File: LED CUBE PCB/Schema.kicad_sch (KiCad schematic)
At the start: 1 part

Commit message: Push changes
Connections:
- net DIN8: now reaches TXB2.11 (B8)
- net DIN7: now reaches TXB2.12 (B7)
- net DIN6: now reaches TXB2.13 (B6)
- net DIN5: now reaches TXB2.14 (B5)
- net GND: now reaches TXB2.15 (GND)
- net DIN4: now reaches TXB2.17 (B4)
- net DIN3: now reaches TXB2.18 (B3)
- net DIN2: now reaches TXB2.19 (B2)
- net DIN1: now reaches TXB2.20 (B1)
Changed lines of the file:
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@@
 (kicad_sch (version 20230121) (generator eeschema)
   (paper "A4")
+  (wire (pts (xy 153.67 63.5) (xy 156.21 63.5))
+    (stroke (width 0) (type default))
+  )
+  (wire (pts (xy 153.67 52.07) (xy 153.67 53.34))
+    (stroke (width 0) (type default))
+  )
   (wire (pts (xy 120.65 57.15) (xy 109.22 57.15))
     (stroke (width 0) (type default))
   )
+  (wire (pts (xy 154.94 41.91) (xy 154.94 40.64))
+    (stroke (width 0) (type default))
+  )
+  (wire (pts (xy 153.67 58.42) (xy 156.21 58.42))
+    (stroke (width 0) (type default))
+  )
+  (wire (pts (xy 138.43 39.37) (xy 154.94 39.37))
+    (stroke (width 0) (type default))
+  )
   (wire (pts (xy 120.65 39.37) (xy 107.95 39.37))
     (stroke (width 0) (type default))
@@
     (stroke (width 0) (type default))
   )
+  (wire (pts (xy 154.94 43.18) (xy 156.21 43.18))
+    (stroke (width 0) (type default))
+  )
+  (wire (pts (xy 153.67 54.61) (xy 153.67 55.88))
+    (stroke (width 0) (type default))
+  )
   (wire (pts (xy 120.65 59.69) (xy 110.49 59.69))
     (stroke (width 0) (type default))
   )
+  (wire (pts (xy 153.67 53.34) (xy 156.21 53.34))
+    (stroke (width 0) (type default))
+  )
+  (wire (pts (xy 153.67 62.23) (xy 153.67 63.5))
+    (stroke (width 0) (type default))
+  )
   (wire (pts (xy 106.68 43.18) (xy 107.95 43.18))
     (stroke (width 0) (type default))
   )
+  (wire (pts (xy 153.67 59.69) (xy 153.67 60.96))
+    (stroke (width 0) (type default))
+  )
+  (wire (pts (xy 138.43 59.69) (xy 153.67 59.69))
+    (stroke (width 0) (type default))
+  )
   (wire (pts (xy 106.68 63.5) (xy 111.76 63.5))
     (stroke (width 0) (type default))
   )
+  (wire (pts (xy 154.94 39.37) (xy 154.94 36.83))
+    (stroke (width 0) (type default))
+  )
   (wire (pts (xy 120.65 54.61) (xy 107.95 54.61))
     (stroke (width 0) (type default))
   )
+  (wire (pts (xy 138.43 52.07) (xy 153.67 52.07))
+    (stroke (width 0) (type default))
+  )
   (wire (pts (xy 106.68 58.42) (xy 109.22 58.42))
     (stroke (width 0) (type default))
@@
     (stroke (width 0) (type default))
   )
+  (wire (pts (xy 154.94 40.64) (xy 156.21 40.64))
+    (stroke (width 0) (type default))
+  )
+  (wire (pts (xy 138.43 46.99) (xy 154.94 46.99))
+    (stroke (width 0) (type default))
+  )
   (wire (pts (xy 106.68 55.88) (xy 107.95 55.88))
     (stroke (width 0) (type default))
@@
     (stroke (width 0) (type default))
   )
+  (wire (pts (xy 153.67 60.96) (xy 156.21 60.96))
+    (stroke (width 0) (type default))
+  )
   (wire (pts (xy 107.95 41.91) (xy 107.95 40.64))
     (stroke (width 0) (type default))
   )
+  (wire (pts (xy 154.94 45.72) (xy 156.21 45.72))
+    (stroke (width 0) (type default))
+  )
   (wire (pts (xy 106.68 60.96) (xy 110.49 60.96))
     (stroke (width 0) (type default))
   )
+  (wire (pts (xy 154.94 46.99) (xy 154.94 45.72))
+    (stroke (width 0) (type default))
+  )
   (wire (pts (xy 120.65 44.45) (xy 107.95 44.45))
     (stroke (width 0) (type default))
@@
     (stroke (width 0) (type default))
   )
+  (wire (pts (xy 138.43 54.61) (xy 153.67 54.61))
+    (stroke (width 0) (type default))
+  )
   (wire (pts (xy 120.65 62.23) (xy 111.76 62.23))
     (stroke (width 0) (type default))
   )
+  (wire (pts (xy 154.94 44.45) (xy 154.94 43.18))
+    (stroke (width 0) (type default))
+  )
+  (wire (pts (xy 138.43 57.15) (xy 153.67 57.15))
+    (stroke (width 0) (type default))
+  )
   (wire (pts (xy 107.95 39.37) (xy 107.95 38.1))
     (stroke (width 0) (type default))
@@
     (stroke (width 0) (type default))
   )
+  (wire (pts (xy 153.67 55.88) (xy 156.21 55.88))
+    (stroke (width 0) (type default))
+  )
   (wire (pts (xy 107.95 54.61) (xy 107.95 55.88))
     (stroke (width 0) (type default))
@@
     (stroke (width 0) (type default))
   )
+  (wire (pts (xy 154.94 36.83) (xy 156.21 36.83))
+    (stroke (width 0) (type default))
+  )
+  (wire (pts (xy 153.67 57.15) (xy 153.67 58.42))
+    (stroke (width 0) (type default))
+  )
   (wire (pts (xy 111.76 62.23) (xy 111.76 63.5))
     (stroke (width 0) (type default))
   )
+  (wire (pts (xy 138.43 44.45) (xy 154.94 44.45))
+    (stroke (width 0) (type default))
+  )
+  (wire (pts (xy 138.43 41.91) (xy 154.94 41.91))
+    (stroke (width 0) (type default))
+  )
   (wire (pts (xy 107.95 44.45) (xy 107.95 43.18))
     (stroke (width 0) (type default))
@@
     (stroke (width 0) (type default))
   )
+  (wire (pts (xy 138.43 62.23) (xy 153.67 62.23))
+    (stroke (width 0) (type default))
+  )
+  (global_label "GND" (shape input) (at 156.21 53.34 0) (fields_autoplaced)
+    (effects (font (size 1.27 1.27)) (justify left))
+    (property "Intersheetrefs" "${INTERSHEET_REFS}" (at 163.0657 53.34 0)
+      (effects (font (size 1.27 1.27)) (justify left) hide)
+    )
+  )
   (global_label "PB5" (shape input) (at 106.68 58.42 180) (fields_autoplaced)
     (effects (font (size 1.27 1.27)) (justify right))
@@
     )
   )
+  (global_label "DIN4" (shape input) (at 156.21 45.72 0) (fields_autoplaced)
+    (effects (font (size 1.27 1.27)) (justify left))
+    (property "Intersheetrefs" "${INTERSHEET_REFS}" (at 163.61 45.72 0)
+      (effects (font (size 1.27 1.27)) (justify left) hide)
+    )
+  )
   (global_label "PB8" (shape input) (at 106.68 43.18 180) (fields_autoplaced)
     (effects (font (size 1.27 1.27)) (justify right))
@@
     )
   )
+  (global_label "DIN6" (shape input) (at 156.21 58.42 0) (fields_autoplaced)
+    (effects (font (size 1.27 1.27)) (justify left))
+    (property "Intersheetrefs" "${INTERSHEET_REFS}" (at 163.61 58.42 0)
+      (effects (font (size 1.27 1.27)) (justify left) hide)
+    )
+  )
+  (global_label "DIN1" (shape input) (at 156.21 36.83 0) (fields_autoplaced)
+    (effects (font (size 1.27 1.27)) (justify left))
+    (property "Intersheetrefs" "${INTERSHEET_REFS}" (at 163.61 36.83 0)
+      (effects (font (size 1.27 1.27)) (justify left) hide)
+    )
+  )
+  (global_label "DIN7" (shape input) (at 156.21 60.96 0) (fields_autoplaced)
+    (effects (font (size 1.27 1.27)) (justify left))
+    (property "Intersheetrefs" "${INTERSHEET_REFS}" (at 163.61 60.96 0)
+      (effects (font (size 1.27 1.27)) (justify left) hide)
+    )
+  )
   (global_label "PB7" (shape input) (at 106.68 45.72 180) (fields_autoplaced)
     (effects (font (size 1.27 1.27)) (justify right))
@@
     )
   )
+  (global_label "DIN5" (shape input) (at 156.21 55.88 0) (fields_autoplaced)
+    (effects (font (size 1.27 1.27)) (justify left))
+    (property "Intersheetrefs" "${INTERSHEET_REFS}" (at 163.61 55.88 0)
+      (effects (font (size 1.27 1.27)) (justify left) hide)
+    )
+  )
+  (global_label "DIN8" (shape input) (at 156.21 63.5 0) (fields_autoplaced)
+    (effects (font (size 1.27 1.27)) (justify left))
+    (property "Intersheetrefs" "${INTERSHEET_REFS}" (at 163.61 63.5 0)
+      (effects (font (size 1.27 1.27)) (justify left) hide)
+    )
+  )
+  (global_label "DIN2" (shape input) (at 156.21 40.64 0) (fields_autoplaced)
+    (effects (font (size 1.27 1.27)) (justify left))
+    (property "Intersheetrefs" "${INTERSHEET_REFS}" (at 163.61 40.64 0)
+      (effects (font (size 1.27 1.27)) (justify left) hide)
+    )
+  )
   (global_label "PB9" (shape input) (at 106.68 40.64 180) (fields_autoplaced)
     (effects (font (size 1.27 1.27)) (justify right))
@@
     )
   )
+  (global_label "DIN3" (shape input) (at 156.21 43.18 0) (fields_autoplaced)
+    (effects (font (size 1.27 1.27)) (justify left))
+    (property "Intersheetrefs" "${INTERSHEET_REFS}" (at 163.61 43.18 0)
+      (effects (font (size 1.27 1.27)) (justify left) hide)
+    )
+  )

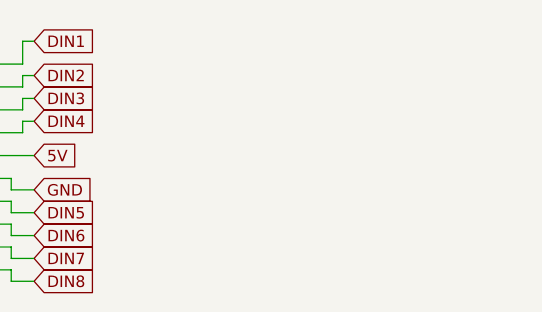
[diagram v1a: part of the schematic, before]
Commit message: Fixed problems on schematic
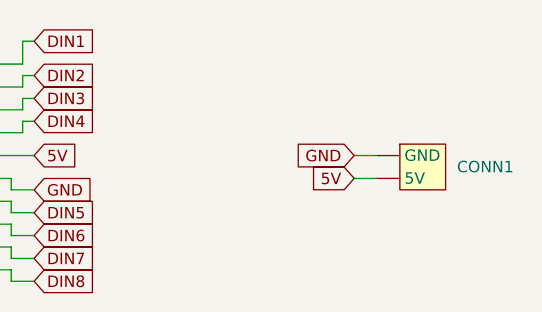
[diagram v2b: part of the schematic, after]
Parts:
- added CONN1: POWER_SUPPLY, Connector_PinSocket_2.54mm:PinSocket_1x02_P2.54mm_Vertical, symbol POWER_SUPPLY:U
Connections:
- net 5V: now also CONN1. (GND)
- net GND: now also CONN1. (GND)

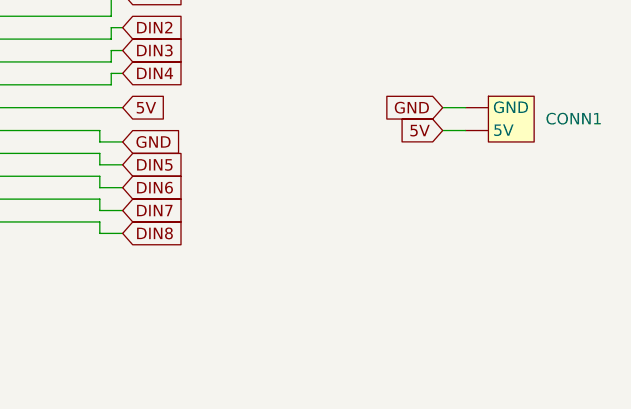
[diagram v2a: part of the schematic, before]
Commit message: Added filtering for power supply
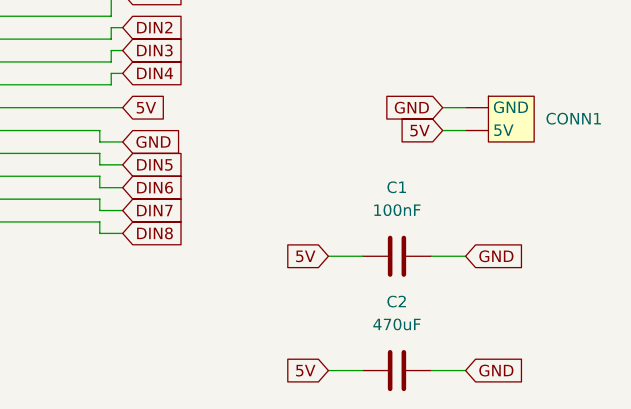
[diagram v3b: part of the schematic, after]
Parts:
- added C1: 100nF, Borna KiCAD Library:C0603, symbol Device:C
- added C2: 470uF, Borna KiCAD Library:C0603, symbol Device:C
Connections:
- net 5V: now also C1.2, C2.2
- net GND: now also C1.1, C2.1

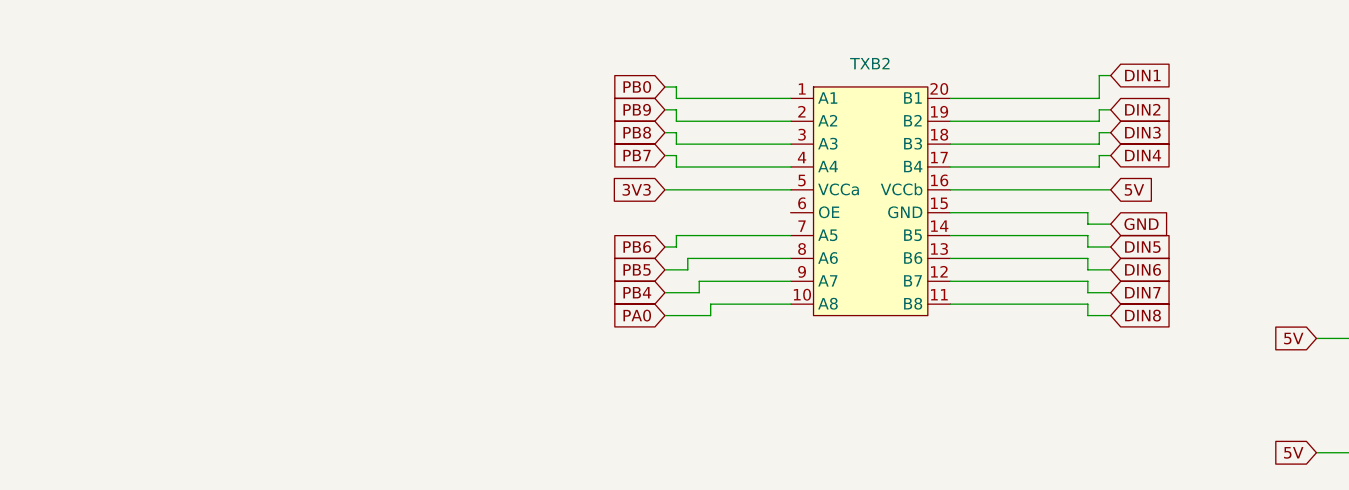
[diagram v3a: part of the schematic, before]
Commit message: Connected voltage regulator and logic level converter
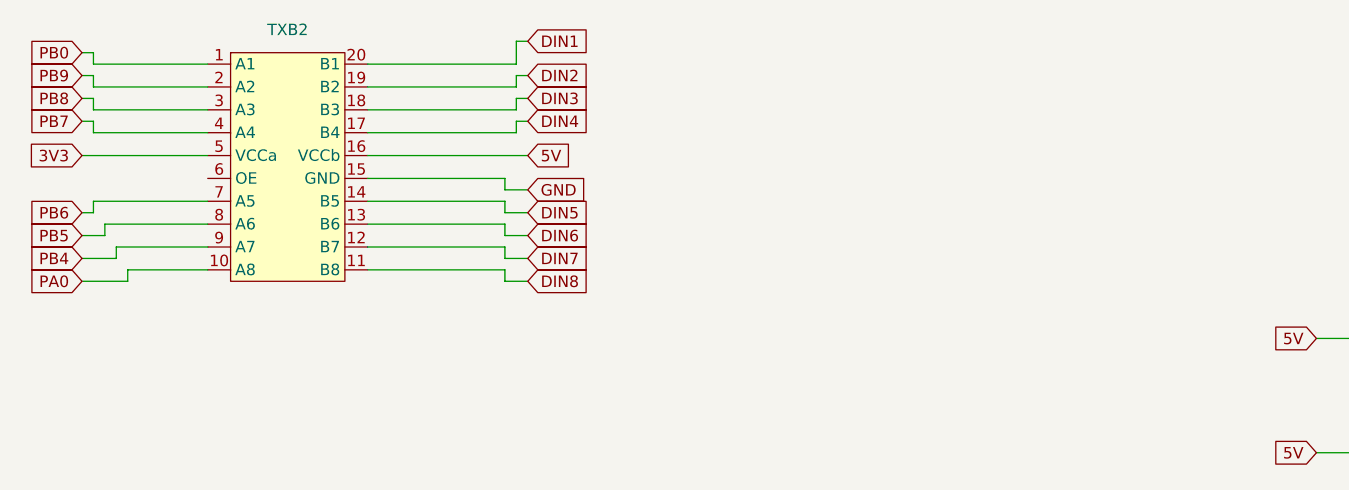
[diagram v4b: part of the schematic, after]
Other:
- moved on the sheet: TXB2

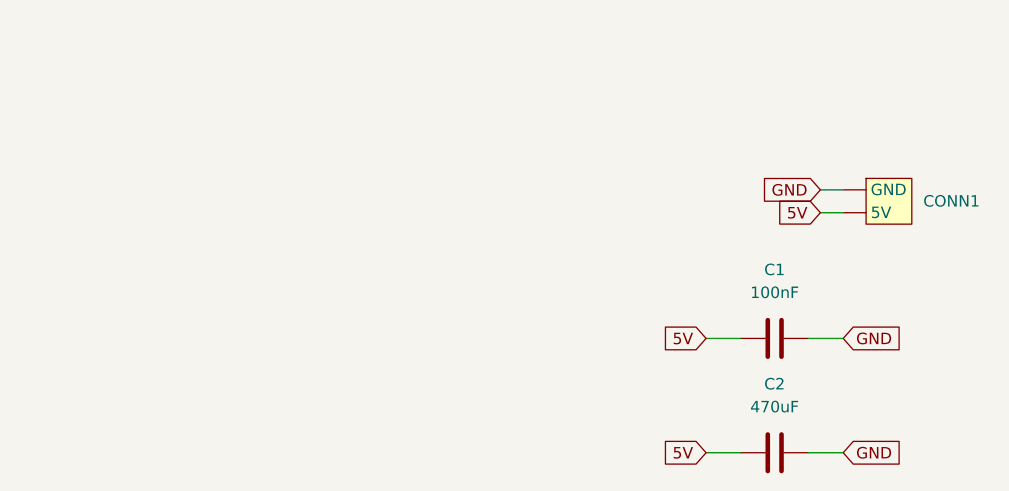
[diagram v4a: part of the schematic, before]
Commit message: Added USB C and CH340C
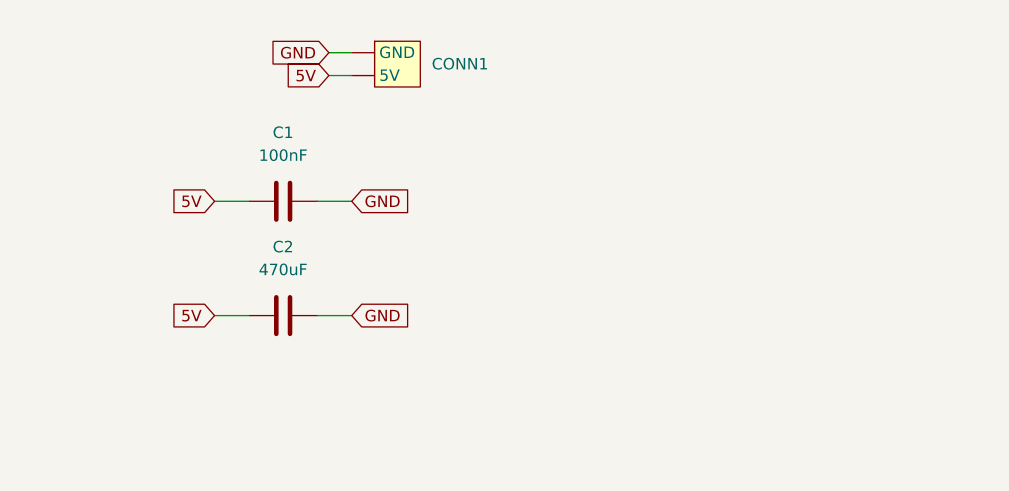
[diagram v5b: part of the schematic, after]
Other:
- moved on the sheet: C1, C2, CONN1
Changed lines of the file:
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@@
 	(wire
 		(pts
-			(xy 191.77 52.07) (xy 194.31 52.07)
+			(xy 137.16 36.83) (xy 139.7 36.83)
 		)
 		(stroke
@@
 	(wire
 		(pts
-			(xy 179.07 78.74) (xy 182.88 78.74)
+			(xy 124.46 63.5) (xy 128.27 63.5)
 		)
 		(stroke
@@
 	(wire
 		(pts
-			(xy 179.07 66.04) (xy 182.88 66.04)
+			(xy 124.46 50.8) (xy 128.27 50.8)
 		)
 		(stroke
@@
 	(wire
 		(pts
-			(xy 190.5 66.04) (xy 194.31 66.04)
+			(xy 135.89 50.8) (xy 139.7 50.8)
 		)
 		(stroke
@@
 	(wire
 		(pts
-			(xy 190.5 78.74) (xy 194.31 78.74)
+			(xy 135.89 63.5) (xy 139.7 63.5)
 		)
 		(stroke
@@
 	(wire
 		(pts
-			(xy 191.77 49.53) (xy 194.31 49.53)
+			(xy 137.16 34.29) (xy 139.7 34.29)
 		)
 		(stroke
@@
 	(global_label "GND"
 		(shape input)
-		(at 194.31 78.74 0)
+		(at 139.7 63.5 0)
 		(fields_autoplaced yes)
 		(effects
@@
 		)
 		(property "Intersheetrefs" "${INTERSHEET_REFS}"
-			(at 201.1657 78.74 0)
+			(at 146.5557 63.5 0)
 			(effects
 				(font
@@
 	(global_label "5V"
 		(shape input)
-		(at 191.77 52.07 180)
+		(at 137.16 36.83 180)
 		(fields_autoplaced yes)
 		(effects
@@
 		)
 		(property "Intersheetrefs" "${INTERSHEET_REFS}"
-			(at 186.4867 52.07 0)
+			(at 131.8767 36.83 0)
 			(effects
 				(font
@@
 	(global_label "5V"
 		(shape input)
-		(at 179.07 66.04 180)
+		(at 124.46 50.8 180)
 		(fields_autoplaced yes)
 		(effects
@@
 		)
 		(property "Intersheetrefs" "${INTERSHEET_REFS}"
-			(at 173.7867 66.04 0)
+			(at 119.1767 50.8 0)
 			(effects
 				(font
@@
 	(global_label "5V"
 		(shape input)
-		(at 179.07 78.74 180)
+		(at 124.46 63.5 180)
 		(fields_autoplaced yes)
 		(effects
@@
 		)
 		(property "Intersheetrefs" "${INTERSHEET_REFS}"
-			(at 173.7867 78.74 0)
+			(at 119.1767 63.5 0)
 			(effects
 				(font
@@
 	(global_label "GND"
 		(shape input)
-		(at 194.31 66.04 0)
+		(at 139.7 50.8 0)
 		(fields_autoplaced yes)
 		(effects
@@
 		)
 		(property "Intersheetrefs" "${INTERSHEET_REFS}"
-			(at 201.1657 66.04 0)
+			(at 146.5557 50.8 0)
 			(effects
 				(font
@@
 	(global_label "GND"
 		(shape input)
-		(at 191.77 49.53 180)
+		(at 137.16 34.29 180)
 		(fields_autoplaced yes)
 		(effects
@@
 		)
 		(property "Intersheetrefs" "${INTERSHEET_REFS}"
-			(at 184.9143 49.53 0)
+			(at 130.3043 34.29 0)
 			(effects
 				(font
@@
 	(symbol
 		(lib_id "Device:C")
-		(at 186.69 78.74 270)
+		(at 132.08 63.5 270)
 		(unit 1)
 		(exclude_from_sim no)
@@
 		(fields_autoplaced yes)
 		(property "Reference" "C2"
-			(at 186.69 71.12 90)
+			(at 132.08 55.88 90)
 			(effects
 				(font
@@
 		)
 		(property "Value" "470uF"
-			(at 186.69 73.66 90)
+			(at 132.08 58.42 90)
 			(effects
 				(font
@@
 		)
 		(property "Footprint" "Borna KiCAD Library:C0603"
-			(at 182.88 79.7052 0)
+			(at 128.27 64.4652 0)
 			(effects
 				(font
@@
 		)
 		(property "Datasheet" "~"
-			(at 186.69 78.74 0)
+			(at 132.08 63.5 0)
 			(effects
 				(font
@@
 		)
 		(property "Description" ""
-			(at 186.69 78.74 0)
+			(at 132.08 63.5 0)
 			(effects
 				(font
@@
 	(symbol
 		(lib_id "Device:C")
-		(at 186.69 66.04 270)
+		(at 132.08 50.8 270)
 		(unit 1)
 		(exclude_from_sim no)
@@
 		(fields_autoplaced yes)
 		(property "Reference" "C1"
-			(at 186.69 58.42 90)
+			(at 132.08 43.18 90)
 			(effects
 				(font
@@
 		)
 		(property "Value" "100nF"
-			(at 186.69 60.96 90)
+			(at 132.08 45.72 90)
 			(effects
 				(font
@@
 		)
 		(property "Footprint" "Borna KiCAD Library:C0603"
-			(at 182.88 67.0052 0)
+			(at 128.27 51.7652 0)
 			(effects
 				(font
@@
 		)
 		(property "Datasheet" "~"
-			(at 186.69 66.04 0)
+			(at 132.08 50.8 0)
 			(effects
 				(font
@@
 		)
 		(property "Description" ""
-			(at 186.69 66.04 0)
+			(at 132.08 50.8 0)
 			(effects
 				(font
@@
 	(symbol
 		(lib_id "POWER_SUPPLY:U")
-		(at 199.39 50.8 0)
+		(at 144.78 35.56 0)
 		(unit 1)
 		(exclude_from_sim no)
@@
 		(fields_autoplaced yes)
 		(property "Reference" "CONN1"
-			(at 203.2 50.7999 0)
+			(at 148.59 35.5599 0)
 			(effects
 				(font
@@
 		)
 		(property "Value" "POWER_SUPPLY"
-			(at 199.39 56.642 0)
+			(at 144.78 41.402 0)
 			(effects
 				(font
@@
 		)
 		(property "Footprint" "Connector_PinSocket_2.54mm:PinSocket_1x02_P2.54mm_Vertical"
-			(at 199.39 54.61 0)
+			(at 144.78 39.37 0)
 			(effects
 				(font
@@
 		)
 		(property "Datasheet" ""
-			(at 199.39 50.8 0)
+			(at 144.78 35.56 0)
 			(effects
 				(font
@@
 		)
 		(property "Description" ""
-			(at 199.39 50.8 0)
-			(effects
-				(font
+			(at 144.78 35.56 0)
+			(effects
+				(font
